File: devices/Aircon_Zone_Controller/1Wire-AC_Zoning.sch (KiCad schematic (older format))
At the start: 39 parts, among them CON1 BARREL_JACK, J1 RJ45, J2 RJ45, J3 JACK_STEREO, P1 CONN_02X05, P2 CONN_01X02, P6 CONN_01X05, U1 LP2950, U10 G3MB_SSR, U11 G3MB_SSR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

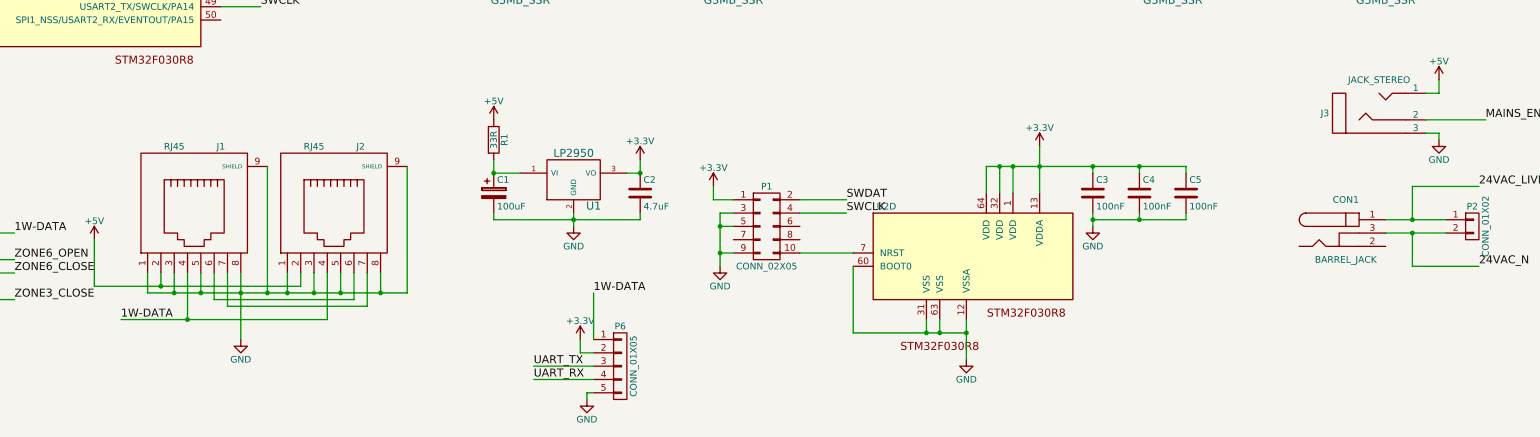
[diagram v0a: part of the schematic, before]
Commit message: Bump all active boards to Revision 1.2
- Remove dropping resistor from 5V power line
- Add pullup resistor to Reset line
- Add pin markings to STM32 chip footprint

Signed-off-by: Alastair D'Silva <alastair@d-silva.org>
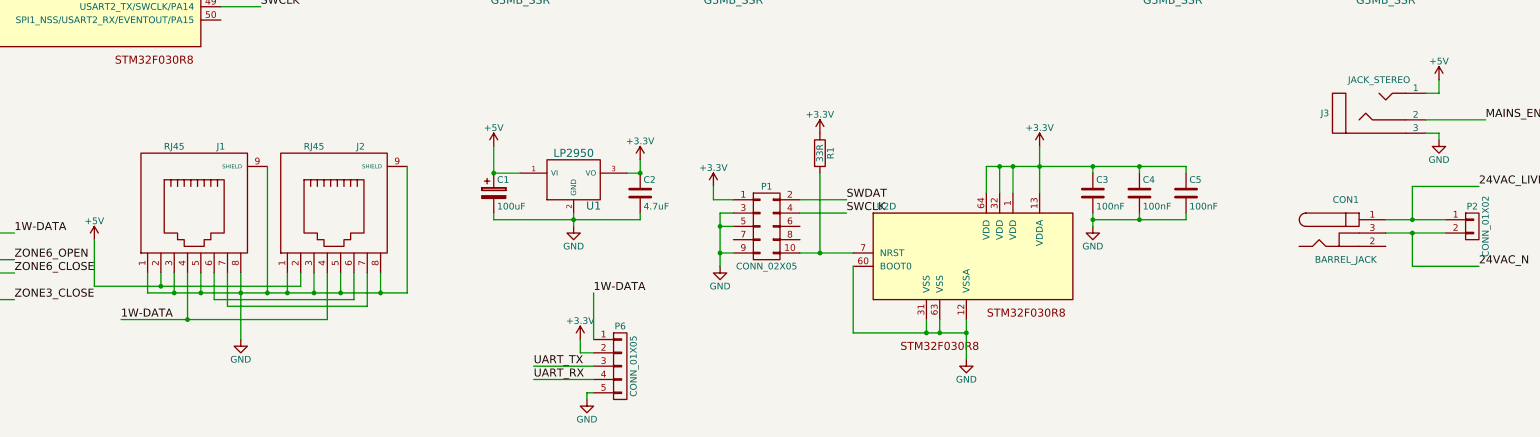
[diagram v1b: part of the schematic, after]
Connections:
- net +3V3: now also R1.1
- net +5V: now also C1.1, U1.1 (VI); no longer R1.1
- net at P1.10 (P10), U2.7 (NRST): now also R1.2
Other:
- moved on the sheet: R1
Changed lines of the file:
@@
-EESchema Schematic File Version 2
+EESchema Schematic File Version 4
+LIBS:1Wire-AC_Zoning-rescue
 LIBS:power
 LIBS:device
@@
 LIBS:Zilog
 LIBS:automotive-light-controller-cache
-LIBS:lp2950
-LIBS:G3MB-SSR
-LIBS:JACK_STEREO
 LIBS:1Wire-AC_Zoning-cache
-EELAYER 25 0
+EELAYER 26 0
 EELAYER END
 $Descr A3 16535 11693
@@
 Sheet 1 1
 Title "1 Wire 8 Zone AC Controller"
-Date "2017-03-09"
-Rev "1.0"
+Date "2018-12-23"
+Rev "1.2"
 Comp "Inferno Embedded"
 Comment1 "Licensed under the TAPR Open Hardware License (www.tapr.org/OHL)"
-Comment2 "Copyright © 2017 Inferno Embedded"
+Comment2 "Copyright © 2018 Inferno Embedded"
 Comment3 ""
 Comment4 ""
@@
 L +5V #PWR07
 U 1 1 5825859A
-P 6650 8700
-F 0 "#PWR07" H 6650 8550 50  0001 C CNN
-F 1 "+5V" H 6650 8840 50  0000 C CNN
-F 2 "" H 6650 8700 50  0000 C CNN
-F 3 "" H 6650 8700 50  0000 C CNN
-	1    6650 8700
+P 6650 8900
+F 0 "#PWR07" H 6650 8750 50  0001 C CNN
+F 1 "+5V" H 6650 9040 50  0000 C CNN
+F 2 "" H 6650 8900 50  0000 C CNN
+F 3 "" H 6650 8900 50  0000 C CNN
+	1    6650 8900
 	1    0    0    -1
 $EndComp
@@
 L R R1
 U 1 1 58B28CDC
-P 6650 8850
-F 0 "R1" V 6730 8850 50  0000 C CNN
-F 1 "33R" V 6650 8850 50  0000 C CNN
-F 2 "Resistors_SMD:R_0603" V 6580 8850 50  0001 C CNN
-F 3 "" H 6650 8850 50  0000 C CNN
-	1    6650 8850
+P 9100 8950
+F 0 "R1" V 9180 8950 50  0000 C CNN
+F 1 "33R" V 9100 8950 50  0000 C CNN
+F 2 "Resistors_SMD:R_0603" V 9030 8950 50  0001 C CNN
+F 3 "" H 9100 8950 50  0000 C CNN
+	1    9100 8950
 	1    0    0    -1
 $EndComp
@@
 	4050 9850 4050 10000
 Wire Wire Line
-	4050 10000 6000 10000
-Wire Wire Line
-	4750 9850 4750 10350
+	4050 10000 4250 10000
+Wire Wire Line
+	4750 9850 4750 10000
 Connection ~ 4750 10000
 Wire Wire Line
@@
 	4150 9850 4150 9950
 Wire Wire Line
-	3650 9950 5200 9950
+	3650 9950 4150 9950
 Wire Wire Line
 	3650 9950 3650 9600
 Wire Wire Line
-	10200 10200 10200 10500
+	10200 10200 10200 10300
 Wire Wire Line
 	9900 10200 9900 10300
 Wire Wire Line
-	9350 10300 10200 10300
+	9350 10300 9900 10300
 Connection ~ 10200 10300
 Wire Wire Line
@@
 Connection ~ 10000 10300
 Wire Wire Line
-	10750 8900 10750 9250
+	10750 8900 10750 9050
 Wire Wire Line
 	10550 9250 10550 9050
@@
 	8450 9400 8350 9400
 Wire Wire Line
-	8350 9400 8350 9800
+	8350 9400 8350 9500
 Wire Wire Line
 	8450 9500 8350 9500
@@
 	4350 9850 4350 10200
 Wire Wire Line
-	3850 10200 5400 10200
+	3850 10200 4350 10200
 Wire Wire Line
 	7650 9100 7750 9100
@@
 	6850 9100 6650 9100
 Wire Wire Line
-	6650 9100 6650 9000
-Wire Wire Line
 	6650 9400 6650 9450
 Wire Wire Line
-	6650 9450 7750 9450
+	6650 9450 7250 9450
 Wire Wire Line
 	7750 9450 7750 9400
 Connection ~ 7250 9450
 Wire Wire Line
-	11150 9400 11150 9500
+	11150 9400 11150 9450
 Wire Wire Line
 	11500 9400 11500 9450
@@
 Connection ~ 9900 10300
 Wire Wire Line
-	10350 9050 11850 9050
-Wire Wire Line
-	11150 9450 11850 9450
+	10350 9050 10450 9050
+Wire Wire Line
+	11150 9450 11500 9450
 Wire Wire Line
 	11850 9050 11850 9100
@@
 	5700 10100 5700 9850
 Wire Wire Line
-	7250 9500 7250 9400
+	7250 9500 7250 9450
 Wire Wire Line
 	6950 10550 7400 10550
@@
 	2800 9550 3050 9550
 Wire Wire Line
-	9350 9700 8950 9700
+	9350 9700 9100 9700
 Wire Wire Line
 	5950 1700 5950 1850
@@
 	12500 7000 12500 7450
 Wire Wire Line
-	13350 9450 13800 9450
-Wire Wire Line
-	13350 9550 13800 9550
+	13350 9450 13550 9450
+Wire Wire Line
+	13350 9550 13550 9550
 Wire Wire Line
 	13550 9550 13550 9800
@@
 Wire Wire Line
 	4600 7550 4900 7550
+Wire Wire Line
+	4750 10000 4950 10000
+Wire Wire Line
+	4750 10000 4750 10350
+Wire Wire Line
+	4250 10000 4450 10000
+Wire Wire Line
+	4450 10000 4750 10000
+Wire Wire Line
+	10200 10300 10200 10500
+Wire Wire Line
+	10000 10300 10200 10300
+Wire Wire Line
+	10750 9050 10750 9250
+Wire Wire Line
+	10750 9050 11150 9050
+Wire Wire Line
+	10550 9050 10750 9050
+Wire Wire Line
+	10450 9050 10550 9050
+Wire Wire Line
+	8350 9500 8350 9700
+Wire Wire Line
+	8350 9700 8350 9800
+Wire Wire Line
+	7250 9450 7750 9450
+Wire Wire Line
+	7250 9450 7250 9400
+Wire Wire Line
+	11150 9450 11150 9500
+Wire Wire Line
+	11150 9050 11500 9050
+Wire Wire Line
+	4950 10000 5100 10000
+Wire Wire Line
+	5100 10000 5300 10000
+Wire Wire Line
+	5300 10000 5500 10000
+Wire Wire Line
+	5500 10000 5800 10000
+Wire Wire Line
+	5800 10000 6000 10000
+Wire Wire Line
+	4150 9950 5200 9950
+Wire Wire Line
+	9900 10300 10000 10300
+Wire Wire Line
+	11500 9050 11850 9050
+Wire Wire Line
+	11500 9450 11850 9450
+Wire Wire Line
+	4350 10200 5400 10200
+Wire Wire Line
+	13550 9550 13800 9550
+Wire Wire Line
+	13550 9450 13800 9450
+Wire Wire Line
+	6650 8900 6650 9100
+Wire Wire Line
+	9100 9100 9100 9700
+Connection ~ 9100 9700
+Wire Wire Line
+	9100 9700 8950 9700
+$Comp
+L +3.3V #PWR?
+U 1 1 5C21E5EC
+P 9100 8800
+F 0 "#PWR?" H 9100 8650 50  0001 C CNN
+F 1 "+3.3V" H 9100 8940 50  0000 C CNN
+F 2 "" H 9100 8800 50  0000 C CNN
+F 3 "" H 9100 8800 50  0000 C CNN
+	1    9100 8800
+	1    0    0    -1
+$EndComp
 $EndSCHEMATC

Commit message: Update AC Zone Controller to KiCAD 5
Signed-off-by: Alastair D'Silva <alastair@d-silva.org>
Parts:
- C1: symbol CP -> Device:CP
- C2, C3, C4, C5: symbol C -> Device:C
- CON1: symbol BARREL_JACK -> conn:BARREL_JACK
- J1, J2, ZONE0, ZONE1, ZONE2, ZONE3, ZONE4, ZONE5, ZONE6, ZONE7: symbol RJ45 -> conn:RJ45
- J3: symbol JACK_STEREO -> 1Wire-AC_Zoning-rescue:JACK_STEREO
- P1: symbol CONN_02X05 -> conn:CONN_02X05
- P2: symbol CONN_01X02 -> conn:CONN_01X02
- P6: symbol CONN_01X05 -> conn:CONN_01X05
- R1: symbol R -> Device:R
- U1: symbol LP2950 -> 1Wire-AC_Zoning-rescue:LP2950
- U10, U11, U12, U13, U14, U15, U16, U17, U18, U3, U4, U5, U6, U7, U8, U9: symbol G3MB_SSR -> 1Wire-AC_Zoning-rescue:G3MB_SSR
- U2: symbol STM32F030R8 -> automotive-light-controller-cache:STM32F030R8
